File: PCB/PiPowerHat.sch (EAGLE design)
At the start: 48 parts, among them J3 Display, J4 FAN1, K1 PIN20X2, Q1 NX2301P, U1 EEPROM24, U2 INA219AIDCNRSOIC, U3 TSL2561T, U4 DS18B20, U5 DS1820SOIC, U6 74AC125

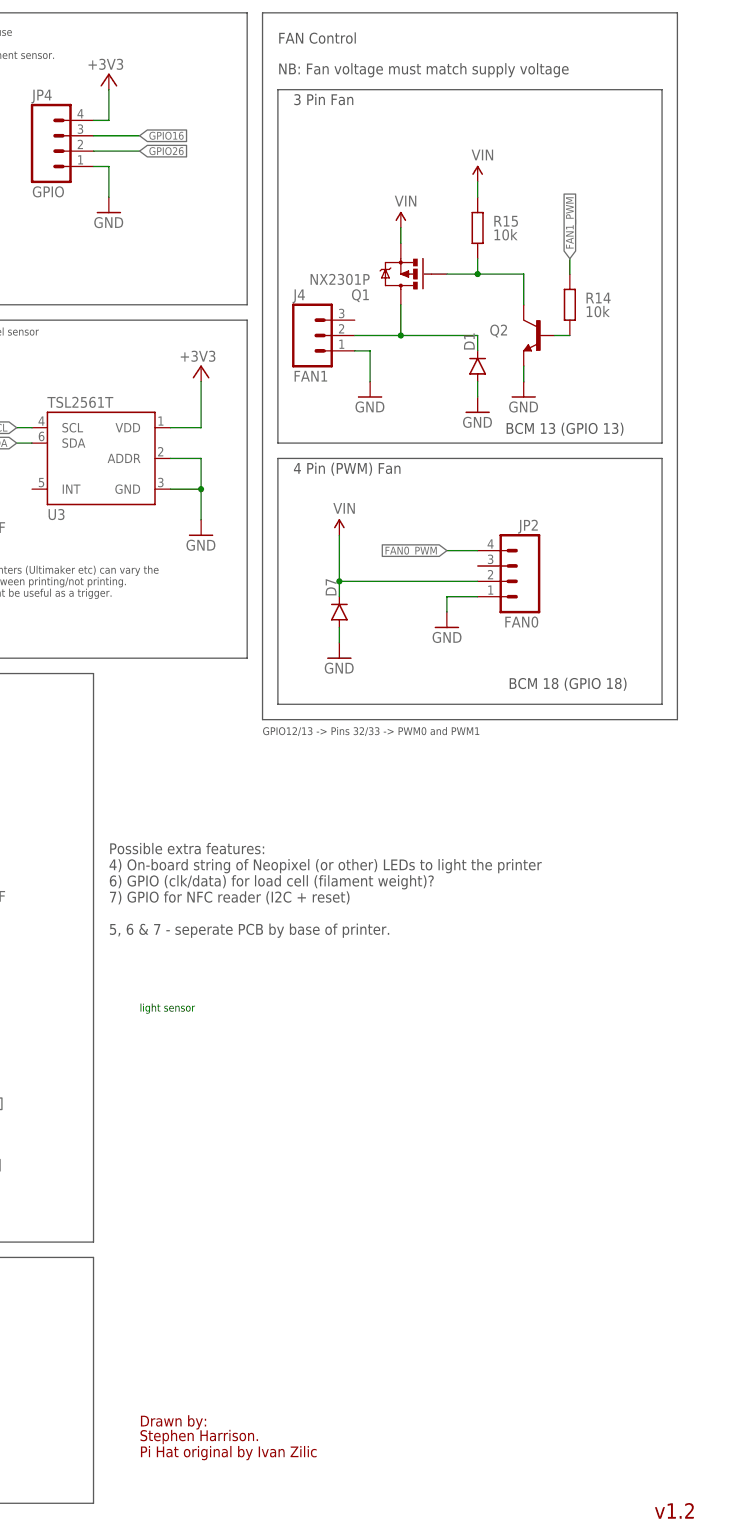
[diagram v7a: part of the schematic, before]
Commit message: Documentation improvements to V1.2 PCB
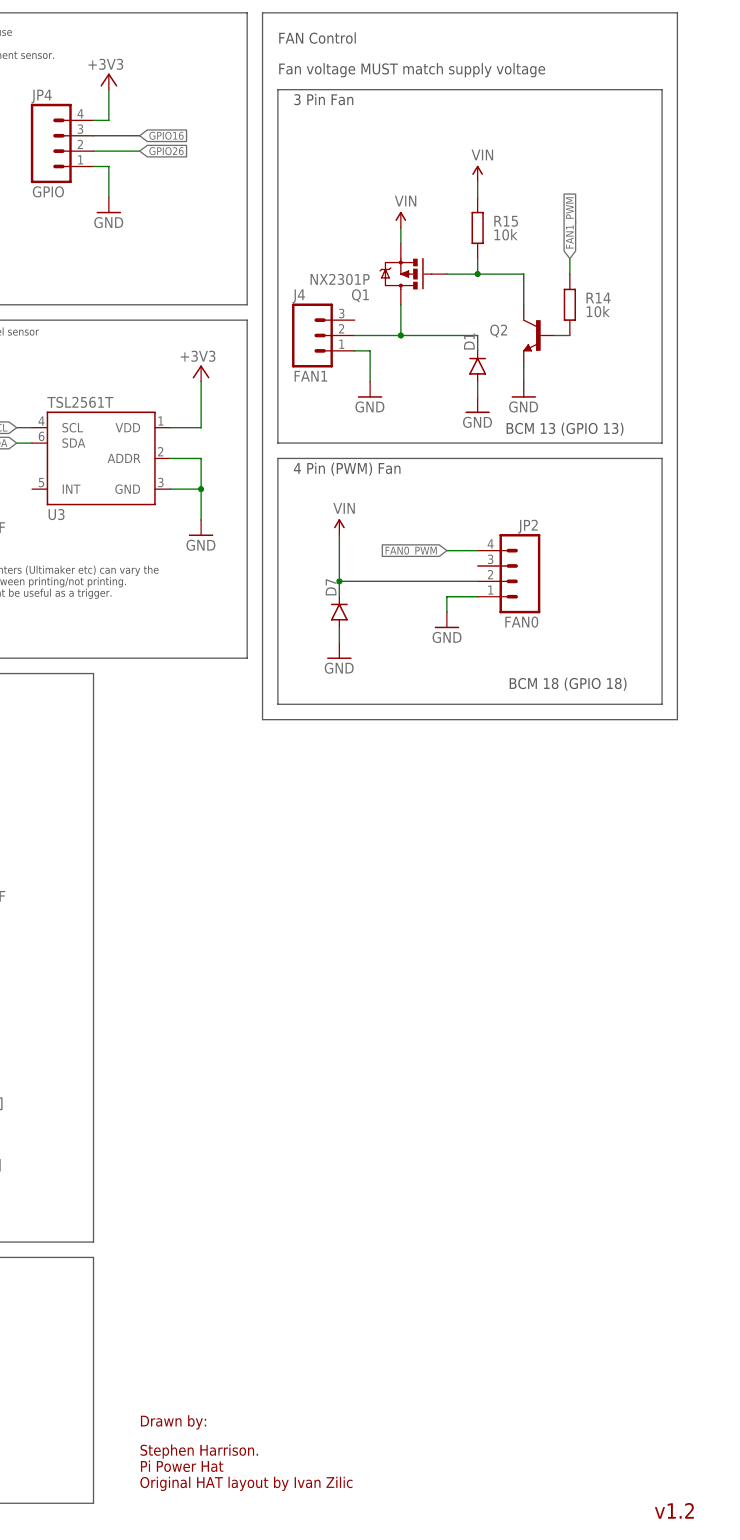
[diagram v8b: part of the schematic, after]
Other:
- note added: "Fan voltage MUST match supply voltage"
- note added: "Stephen Harrison. Pi Power Hat Original HAT layout by Ivan Zilic"
- note removed: "GPIO12/13 -> Pins 32/33 -> PWM0 and PWM1"
- note removed: "NB: Fan voltage must match supply voltage"
- note removed: "Possible extra features: 4) On-board string of Neopixel (or other) LEDs to light the printer 6) GPIO (clk/data) for load cell (filament weight)? 7) GPIO for NFC reader (I2C + reset) 5, 6 & 7 - seperate PCB by base of printer."
- note removed: "Stephen Harrison. Pi Hat original by Ivan Zilic"
- note removed: "light sensor"
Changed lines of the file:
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@@
 <plain>
 <text x="289.56" y="20.32" size="1.778" layer="94" ratio="15">Drawn by:</text>
-<text x="289.56" y="15.24" size="1.778" layer="94">Stephen Harrison.
-Pi Hat original by Ivan Zilic</text>
+<text x="289.56" y="10.16" size="1.778" layer="94">Stephen Harrison.
+Pi Power Hat
+Original HAT layout by Ivan Zilic</text>
 <text x="374.65" y="5.08" size="2.54" layer="94" ratio="10">v1.2</text>
 <text x="185.42" y="167.64" size="1.27" layer="97">SOIC 8 temp sensor to monitor PCB/Ambient.</text>
@@
 NB: This is the same as HTU21D </text>
 <text x="134.62" y="58.42" size="1.27" layer="97">See: https://github.com/scottjw/subfact_pi_ina219</text>
-<text x="284.48" y="101.6" size="1.778" layer="97">Possible extra features:
-4) On-board string of Neopixel (or other) LEDs to light the printer
-6) GPIO (clk/data) for load cell (filament weight)?
-7) GPIO for NFC reader (I2C + reset)
-5, 6 &amp; 7 - seperate PCB by base of printer. </text>
 <text x="193.04" y="162.56" size="1.27" layer="97">GPIO4 is default for 1-Wire</text>
-<text x="309.88" y="134.62" size="1.27" layer="97">GPIO12/13 -&gt; Pins 32/33 -&gt; PWM0 and PWM1</text>
 <wire x1="312.42" y1="139.7" x2="375.92" y2="139.7" width="0.1524" layer="97"/>
 <wire x1="375.92" y1="139.7" x2="375.92" y2="180.34" width="0.1524" layer="97"/>
@@
 <text x="314.96" y="238.76" size="1.778" layer="97">3 Pin Fan</text>
 <text x="314.96" y="177.8" size="1.778" layer="97">4 Pin (PWM) Fan</text>
-<text x="312.42" y="243.84" size="1.778" layer="97">NB: Fan voltage must match supply voltage</text>
+<text x="312.42" y="243.84" size="1.778" layer="97" ratio="12">Fan voltage MUST match supply voltage</text>
 <wire x1="309.88" y1="137.16" x2="309.88" y2="254" width="0.1524" layer="97"/>
 <wire x1="309.88" y1="254" x2="378.46" y2="254" width="0.1524" layer="97"/>
@@
 <wire x1="281.94" y1="7.62" x2="281.94" y2="48.26" width="0.1524" layer="97"/>
 <wire x1="281.94" y1="48.26" x2="7.62" y2="48.26" width="0.1524" layer="97"/>
-<text x="289.56" y="88.9" size="1.27" layer="91">light sensor</text>
 <text x="10.16" y="93.98" size="1.27" layer="97">Also suitable for Adafruit small LCD display</text>
 <wire x1="256.54" y1="203.2" x2="307.34" y2="203.2" width="0.1524" layer="97"/>
